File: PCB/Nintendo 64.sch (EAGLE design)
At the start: 21 parts, among them U1A SN74AHCT125N, U2A SN74AHCT125N, U3A SN74AHCT125N, U4A SN74AHCT125N

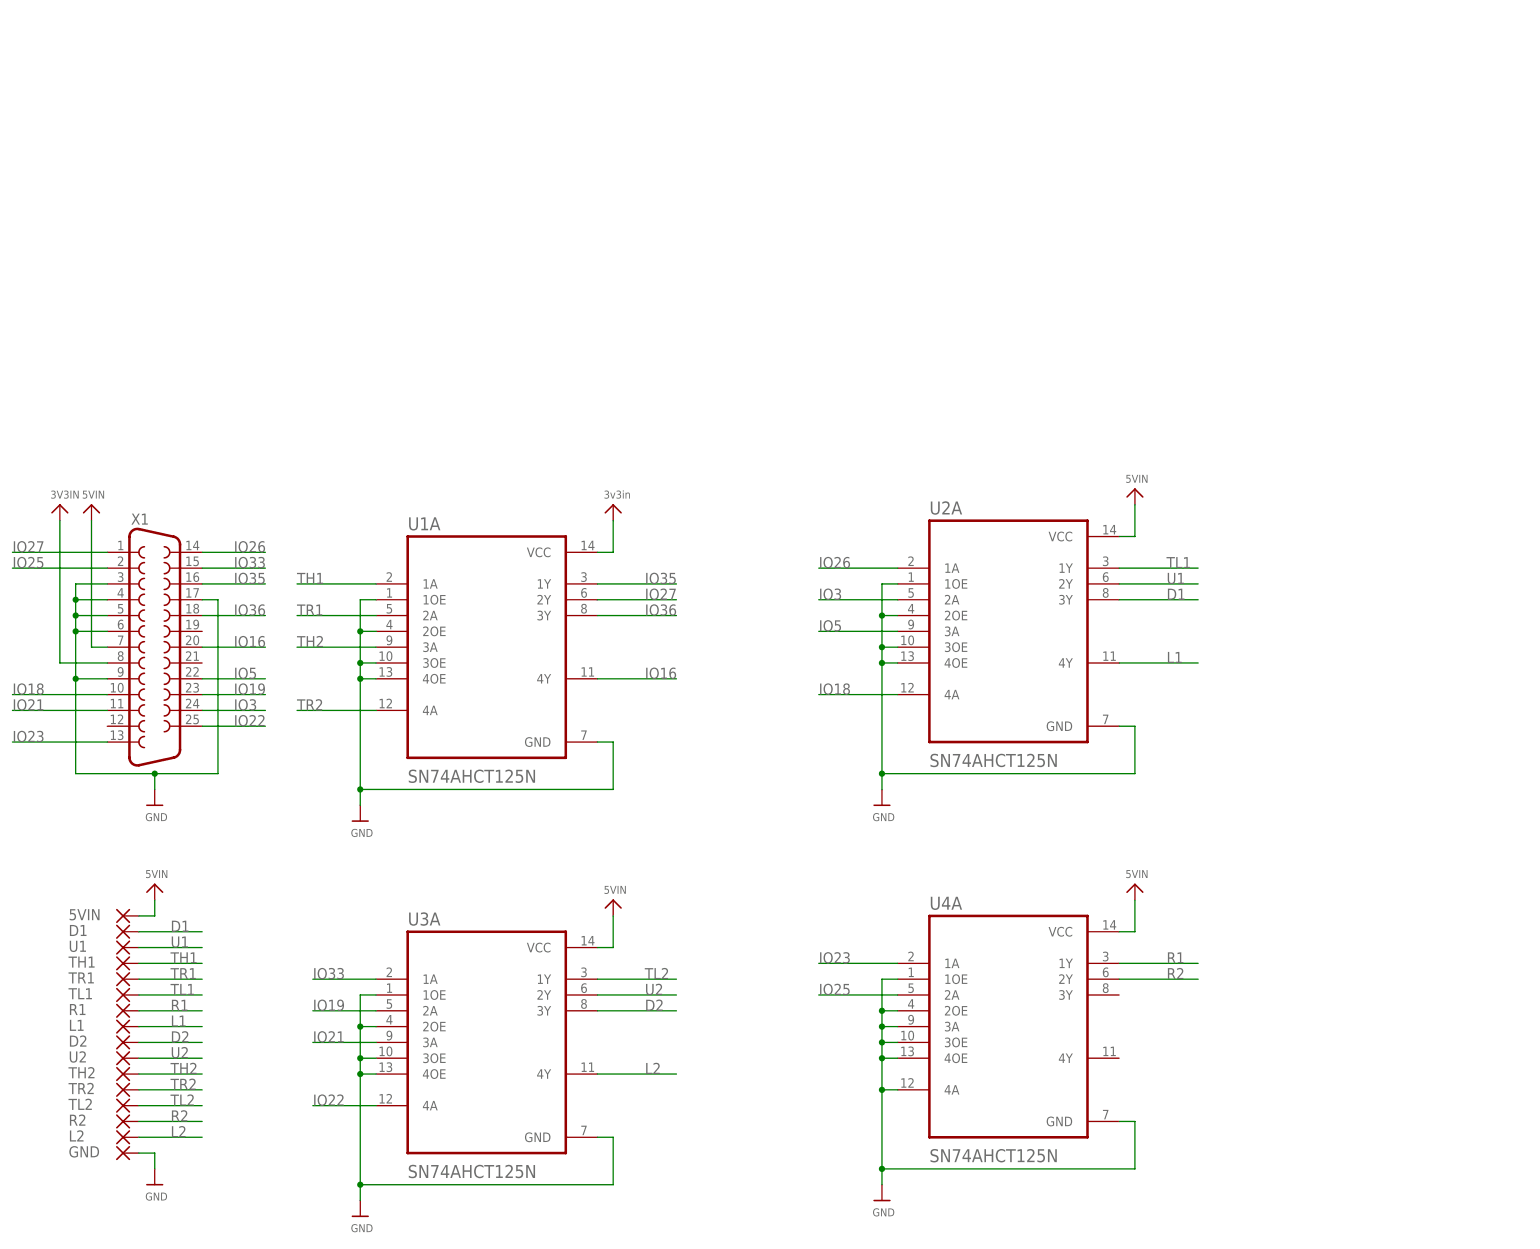
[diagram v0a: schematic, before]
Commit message: PCB Updates/New Additions
All existing PCBs had silkscreen updates and NES, Virtual Boy, PSX/PS2, Nintendo 64, Saturn have been added.
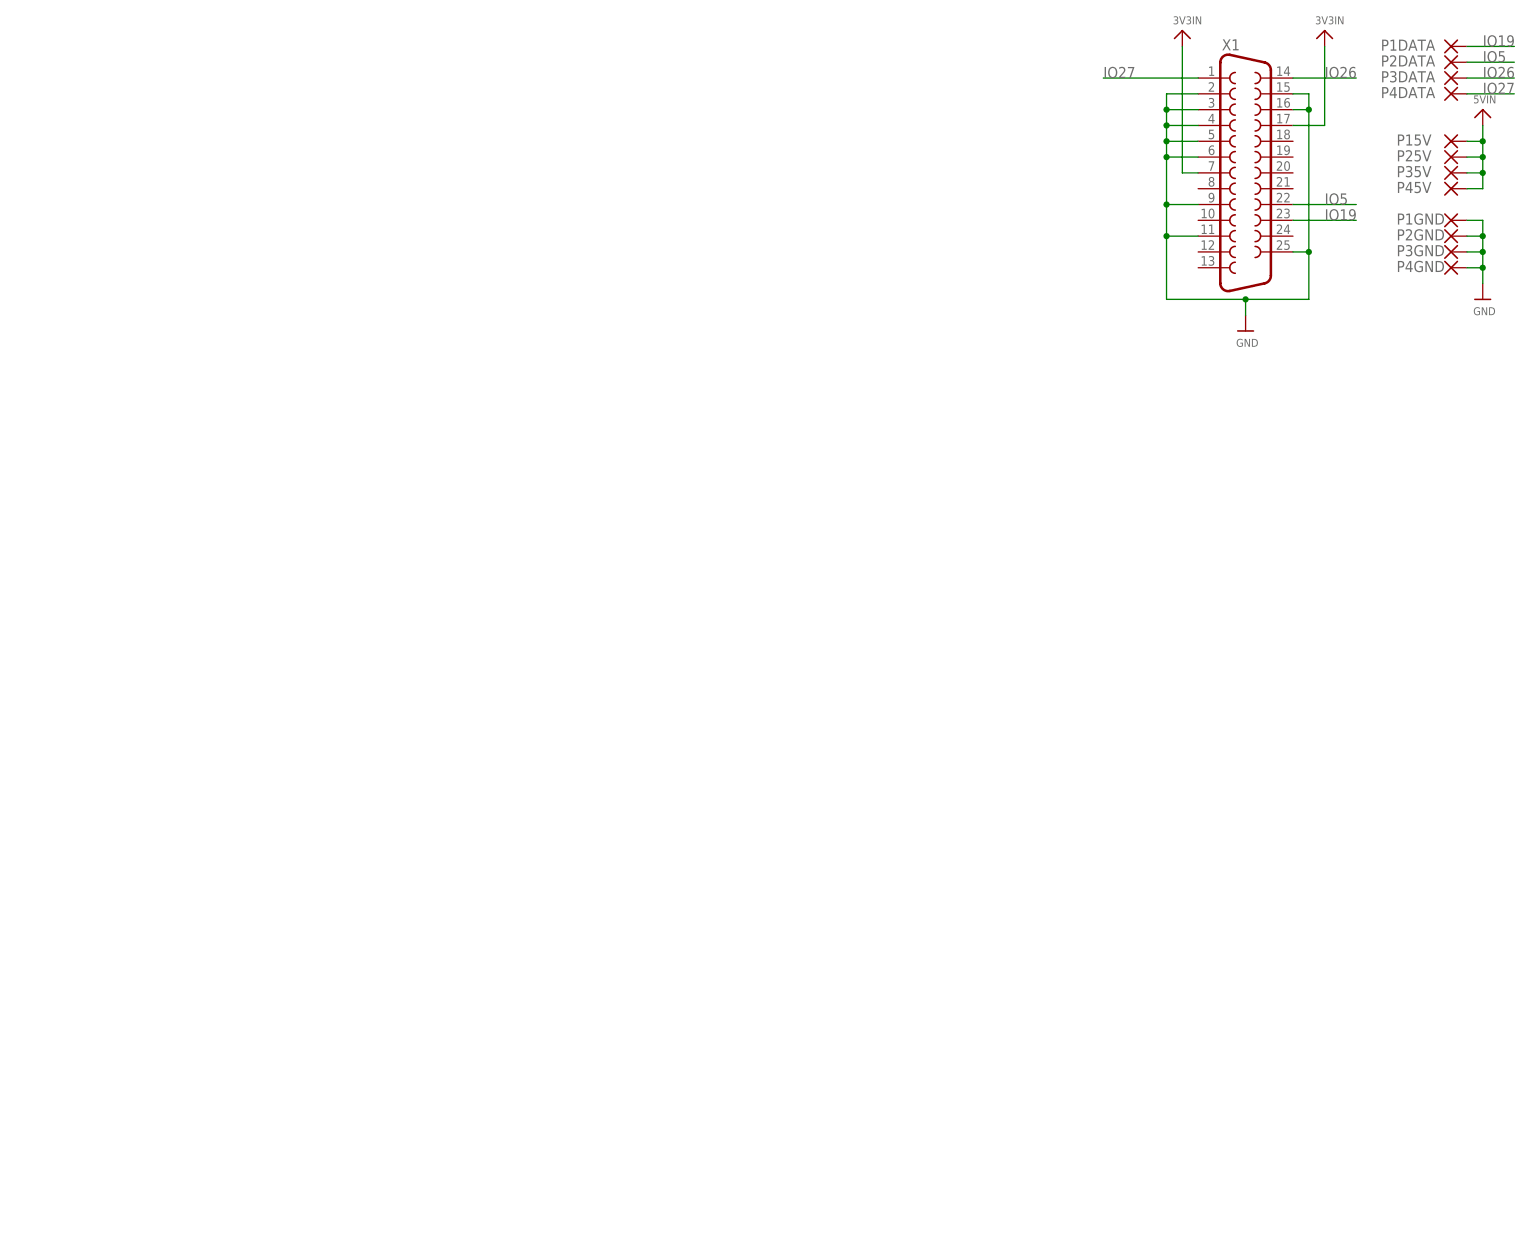
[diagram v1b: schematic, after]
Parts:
- removed 5VIN, D1, D2, GND, L1, L2, R1, R2, TH1, TH2, TL1, TL2, TR1, TR2, U1, U2: (no value), wirepad:SMD5
- removed U1A, U2A, U3A, U4A: SN74AHCT125N, SN74AHCT125N:SN74AHCT125N
- added P15V, P1DATA, P1GND, P25V, P2DATA, P2GND, P35V, P3DATA, P3GND, P45V, P4DATA, P4GND: (no value), wirepad:SMD5
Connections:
- removed net 5VIN: 5VIN.P, U2A.VCC, U3A.VCC, U4A.VCC, X1.7
- removed net D1: D1.P, U2A.3Y
- removed net D2: D2.P, U3A.3Y
- removed net IO16: U1A.4Y, X1.20
- removed net IO18: U2A.4A, X1.10
- removed net IO21: U3A.3A, X1.11
- removed net IO22: U3A.4A, X1.25
- removed net IO23: U4A.1A, X1.13
- removed net IO25: U4A.2A, X1.2
- removed net IO3: U2A.2A, X1.24
- removed net IO33: U3A.1A, X1.15
- removed net IO35: U1A.1Y, X1.16
- removed net IO36: U1A.3Y, X1.18
- removed net L1: L1.P, U2A.4Y
- removed net L2: L2.P, U3A.4Y
- removed net R1: R1.P, U4A.1Y
- removed net R2: R2.P, U4A.2Y
- removed net TH1: TH1.P, U1A.1A
- removed net TH2: TH2.P, U1A.3A
- removed net TL1: TL1.P, U2A.1Y
- removed net TL2: TL2.P, U3A.1Y
- removed net TR1: TR1.P, U1A.2A
- removed net TR2: TR2.P, U1A.4A
- removed net U1: U1.P, U2A.2Y
- removed net U2: U2.P, U3A.2Y
- net 3V3IN: now also P15V.P, P25V.P, P35V.P, P45V.P, X1.17, X1.7; no longer U1A.VCC, X1.8
- net GND: now also P1GND.P, P2GND.P, P3GND.P, P4GND.P, X1.11, X1.15, X1.16, X1.2, X1.25; no longer GND.P, U1A.1OE, U1A.2OE, U1A.3OE, U1A.4OE, U1A.GND, U2A.1OE, U2A.2OE, U2A.3OE, U2A.4OE, U2A.GND, U3A.1OE, U3A.2OE, U3A.3OE, U3A.4OE, U3A.GND, U4A.1OE, U4A.2OE, U4A.3A, U4A.3OE, U4A.4A, U4A.4OE, U4A.GND, X1.17
- net IO19: now also P1DATA.P; no longer U3A.2A
- net IO26: now also P3DATA.P; no longer U2A.1A
- net IO27: now also P4DATA.P; no longer U1A.2Y
- net IO5: now also P2DATA.P; no longer U2A.3A
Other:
- moved on the sheet: X1

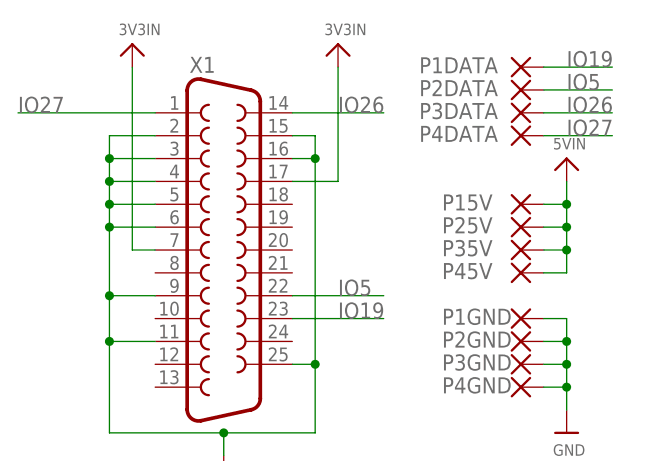
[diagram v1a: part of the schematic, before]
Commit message: Datasheets, BOM Update, 3 New PCBs
Added Datasheets for the Female/Male DB25 connectors
Updated formatting on the BOM

New PCBs:
Added Nintendo 64 (Updated to 1.1, Moved VIN from 5V to 3V3)
Added Sega Saturn (Updated to 1.1, Added 5V and GND Pads on bottom for Second player pads to ease install)
Added NES

Removed PSX/PS2 and Virtual Boy as work is not complete (New branches will be made for each one)
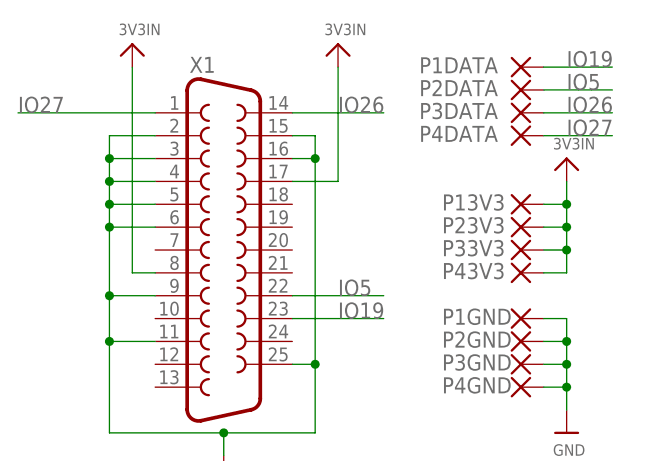
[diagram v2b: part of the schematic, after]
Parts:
- renumbered P15V to P13V3, P25V to P23V3, P35V to P33V3, P45V to P43V3
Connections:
- net 3V3IN: now also X1.8; no longer X1.7
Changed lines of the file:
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@@
 <part name="P3DATA" library="wirepad" library_urn="urn:adsk.eagle:library:412" deviceset="SMD5" device="" package3d_urn="urn:adsk.eagle:package:30841/1"/>
 <part name="P1GND" library="wirepad" library_urn="urn:adsk.eagle:library:412" deviceset="SMD5" device="" package3d_urn="urn:adsk.eagle:package:30841/1"/>
-<part name="P15V" library="wirepad" library_urn="urn:adsk.eagle:library:412" deviceset="SMD5" device="" package3d_urn="urn:adsk.eagle:package:30841/1"/>
+<part name="P13V3" library="wirepad" library_urn="urn:adsk.eagle:library:412" deviceset="SMD5" device="" package3d_urn="urn:adsk.eagle:package:30841/1"/>
 <part name="P4DATA" library="wirepad" library_urn="urn:adsk.eagle:library:412" deviceset="SMD5" device="" package3d_urn="urn:adsk.eagle:package:30841/1"/>
-<part name="P25V" library="wirepad" library_urn="urn:adsk.eagle:library:412" deviceset="SMD5" device="" package3d_urn="urn:adsk.eagle:package:30841/1"/>
-<part name="P35V" library="wirepad" library_urn="urn:adsk.eagle:library:412" deviceset="SMD5" device="" package3d_urn="urn:adsk.eagle:package:30841/1"/>
-<part name="P45V" library="wirepad" library_urn="urn:adsk.eagle:library:412" deviceset="SMD5" device="" package3d_urn="urn:adsk.eagle:package:30841/1"/>
+<part name="P23V3" library="wirepad" library_urn="urn:adsk.eagle:library:412" deviceset="SMD5" device="" package3d_urn="urn:adsk.eagle:package:30841/1"/>
+<part name="P33V3" library="wirepad" library_urn="urn:adsk.eagle:library:412" deviceset="SMD5" device="" package3d_urn="urn:adsk.eagle:package:30841/1"/>
+<part name="P43V3" library="wirepad" library_urn="urn:adsk.eagle:library:412" deviceset="SMD5" device="" package3d_urn="urn:adsk.eagle:package:30841/1"/>
 <part name="P2GND" library="wirepad" library_urn="urn:adsk.eagle:library:412" deviceset="SMD5" device="" package3d_urn="urn:adsk.eagle:package:30841/1"/>
 <part name="P3GND" library="wirepad" library_urn="urn:adsk.eagle:library:412" deviceset="SMD5" device="" package3d_urn="urn:adsk.eagle:package:30841/1"/>
@@
 <part name="P2DATA" library="wirepad" library_urn="urn:adsk.eagle:library:412" deviceset="SMD5" device="" package3d_urn="urn:adsk.eagle:package:30841/1"/>
 <part name="U$52" library="Airquality_Sensor" library_urn="urn:adsk.eagle:library:16015176" deviceset="GND" device=""/>
-<part name="U$55" library="microbuilder" deviceset="VIN" device="" value="5VIN"/>
+<part name="U$55" library="microbuilder" deviceset="VIN" device="" value="3V3IN"/>
 <part name="U$1" library="microbuilder" deviceset="VIN" device="" value="3V3IN"/>
 </parts>
@@
 <attribute name="VALUE" x="445.897" y="-23.622" size="1.778" layer="96"/>
 </instance>
-<instance part="P15V" gate="1" x="447.04" y="-7.62" smashed="yes">
+<instance part="P13V3" gate="1" x="447.04" y="-7.62" smashed="yes">
 <attribute name="NAME" x="438.277" y="-8.3058" size="1.778" layer="95"/>
 <attribute name="VALUE" x="445.897" y="-10.922" size="1.778" layer="96"/>
@@
 <attribute name="VALUE" x="445.897" y="-3.302" size="1.778" layer="96"/>
 </instance>
-<instance part="P25V" gate="1" x="447.04" y="-10.16" smashed="yes">
+<instance part="P23V3" gate="1" x="447.04" y="-10.16" smashed="yes">
 <attribute name="NAME" x="438.277" y="-10.8458" size="1.778" layer="95"/>
 <attribute name="VALUE" x="445.897" y="-13.462" size="1.778" layer="96"/>
 </instance>
-<instance part="P35V" gate="1" x="447.04" y="-12.7" smashed="yes">
+<instance part="P33V3" gate="1" x="447.04" y="-12.7" smashed="yes">
 <attribute name="NAME" x="438.277" y="-13.3858" size="1.778" layer="95"/>
 <attribute name="VALUE" x="445.897" y="-16.002" size="1.778" layer="96"/>
 </instance>
-<instance part="P45V" gate="1" x="447.04" y="-15.24" smashed="yes">
+<instance part="P43V3" gate="1" x="447.04" y="-15.24" smashed="yes">
 <attribute name="NAME" x="438.277" y="-15.9258" size="1.778" layer="95"/>
 <attribute name="VALUE" x="445.897" y="-18.542" size="1.778" layer="96"/>
@@
 <net name="3V3IN" class="0">
 <segment>
-<wire x1="403.86" y1="-12.7" x2="403.86" y2="7.62" width="0.1524" layer="91"/>
+<wire x1="403.86" y1="-15.24" x2="403.86" y2="7.62" width="0.1524" layer="91"/>
 <pinref part="U$53" gate="G$1" pin="VIN"/>
-<pinref part="X1" gate="-1" pin="7"/>
-<wire x1="406.4" y1="-12.7" x2="403.86" y2="-12.7" width="0.1524" layer="91"/>
+<pinref part="X1" gate="-1" pin="8"/>
+<wire x1="406.4" y1="-15.24" x2="403.86" y2="-15.24" width="0.1524" layer="91"/>
 </segment>
 <segment>
@@
 </segment>
 <segment>
-<pinref part="P15V" gate="1" pin="P"/>
-<pinref part="P45V" gate="1" pin="P"/>
+<pinref part="P13V3" gate="1" pin="P"/>
+<pinref part="P43V3" gate="1" pin="P"/>
 <wire x1="452.12" y1="-7.62" x2="449.58" y2="-7.62" width="0.1524" layer="91"/>
 <wire x1="449.58" y1="-15.24" x2="452.12" y2="-15.24" width="0.1524" layer="91"/>
-<pinref part="P35V" gate="1" pin="P"/>
+<pinref part="P33V3" gate="1" pin="P"/>
 <wire x1="449.58" y1="-12.7" x2="452.12" y2="-12.7" width="0.1524" layer="91"/>
-<pinref part="P25V" gate="1" pin="P"/>
+<pinref part="P23V3" gate="1" pin="P"/>
 <wire x1="449.58" y1="-10.16" x2="452.12" y2="-10.16" width="0.1524" layer="91"/>
 <pinref part="U$55" gate="G$1" pin="VIN"/>

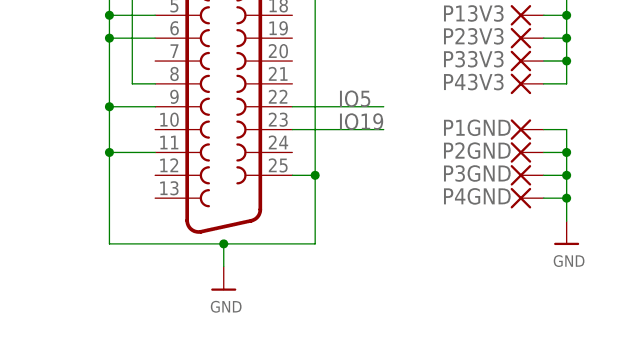
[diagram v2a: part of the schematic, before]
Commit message: Added exposed GND plane at DB25 anchors
All PCBs have been update to have exposed GND plane pads for the DB25 anchor points.

This resolves Issue 54
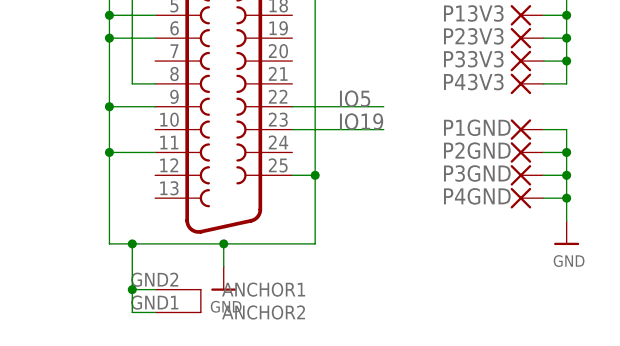
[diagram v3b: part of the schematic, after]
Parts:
- X1: device SparkFun-Retired:DB25_FEMALEH -> SparkFun-Retired:DB25_FEMALEHP
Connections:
- net GND: now also X1.ANCHOR1, X1.ANCHOR2
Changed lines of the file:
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@@
 </classes>
 <parts>
-<part name="X1" library="SparkFun-Retired" deviceset="DB25_FEMALE" device="H"/>
+<part name="X1" library="SparkFun-Retired" deviceset="DB25_FEMALE" device="HP"/>
 <part name="U$53" library="microbuilder" deviceset="VIN" device="" value="3V3IN"/>
 <part name="U$54" library="Airquality_Sensor" library_urn="urn:adsk.eagle:library:16015176" deviceset="GND" device=""/>
@@
 <wire x1="414.02" y1="-33.02" x2="414.02" y2="-35.56" width="0.1524" layer="91"/>
 <junction x="414.02" y="-33.02"/>
-<wire x1="414.02" y1="-33.02" x2="401.32" y2="-33.02" width="0.1524" layer="91"/>
+<wire x1="414.02" y1="-33.02" x2="403.86" y2="-33.02" width="0.1524" layer="91"/>
 <pinref part="X1" gate="-1" pin="2"/>
+<wire x1="403.86" y1="-33.02" x2="401.32" y2="-33.02" width="0.1524" layer="91"/>
 <wire x1="406.4" y1="0" x2="401.32" y2="0" width="0.1524" layer="91"/>
 <wire x1="401.32" y1="0" x2="401.32" y2="-2.54" width="0.1524" layer="91"/>
@@
 <wire x1="421.64" y1="-25.4" x2="424.18" y2="-25.4" width="0.1524" layer="91"/>
 <junction x="424.18" y="-25.4"/>
+<pinref part="X1" gate="-1" pin="ANCHOR2"/>
+<wire x1="406.4" y1="-40.64" x2="403.86" y2="-40.64" width="0.1524" layer="91"/>
+<wire x1="403.86" y1="-40.64" x2="403.86" y2="-38.1" width="0.1524" layer="91"/>
+<junction x="403.86" y="-33.02"/>
+<pinref part="X1" gate="-1" pin="ANCHOR1"/>
+<wire x1="403.86" y1="-38.1" x2="403.86" y2="-33.02" width="0.1524" layer="91"/>
+<wire x1="406.4" y1="-38.1" x2="403.86" y2="-38.1" width="0.1524" layer="91"/>
+<junction x="403.86" y="-38.1"/>
 </segment>
 <segment>
